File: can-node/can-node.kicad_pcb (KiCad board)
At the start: 4 copper layers, 76.3 x 58.9 mm, 139 parts, among them J1 Conn_ARM_JTAG_SWD_10, J2 Conn_01x04_Pin, J3 USART1, J4 Harwin M80-5402642, J5 Harwin M80-5402642, Q1 DMP510DL-7, SW1 KMR2, U1 TCAN3404-Q1, U10 TLV9101IDBVR, U11 TLV9101IDBVR, U12 TLV9101IDBVR, U13 TLV9101IDBVR, U14 TLV9101IDBVR, U15 TLV9101IDBVR, U16 TLV9101IDBVR, U17 TLV9101IDBVR, U18 TLV9101IDBVR, U19 TLV9101IDBVR, U2 STM32F105RBTx, U3 AP7375-33FDC, U4 TLV9101IDBVR, U5 TLV9101IDBVR, U6 TLV9101IDBVR, U7 TLV9101IDBVR, U8 TLV9101IDBVR, U9 TLV9101IDBVR, Y1 ECS-250-10-47Q-CES-TR

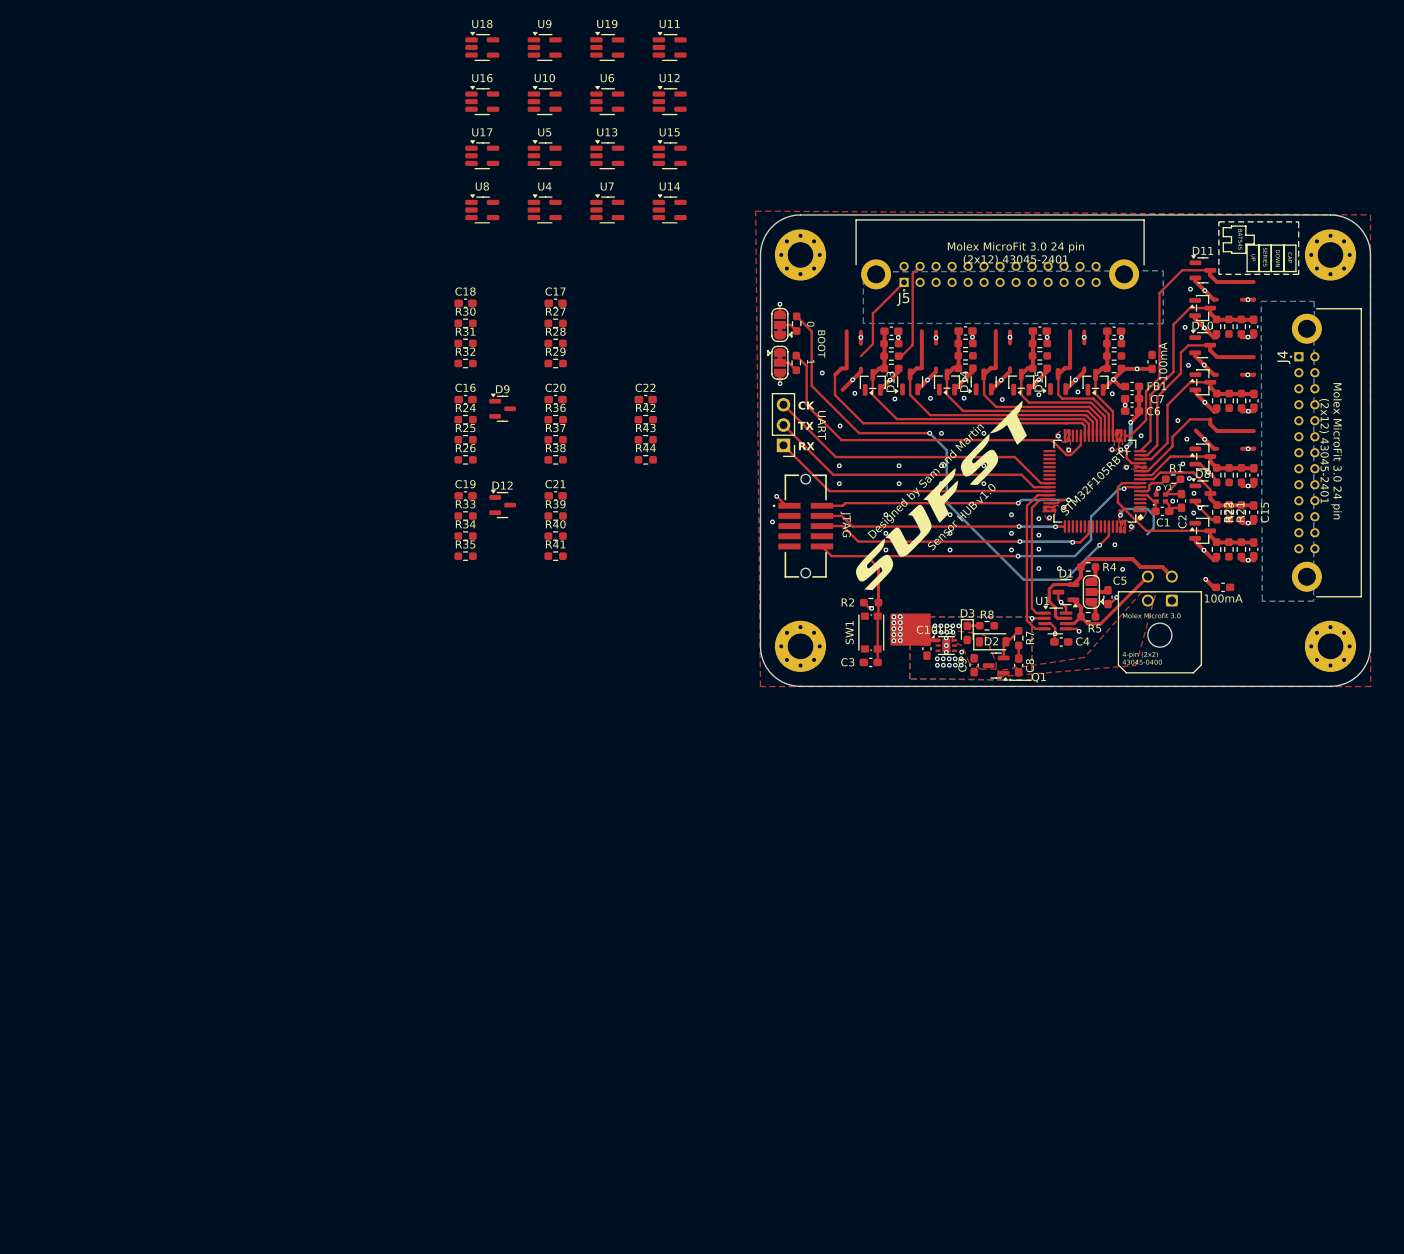
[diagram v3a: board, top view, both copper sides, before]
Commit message: reroute can-node
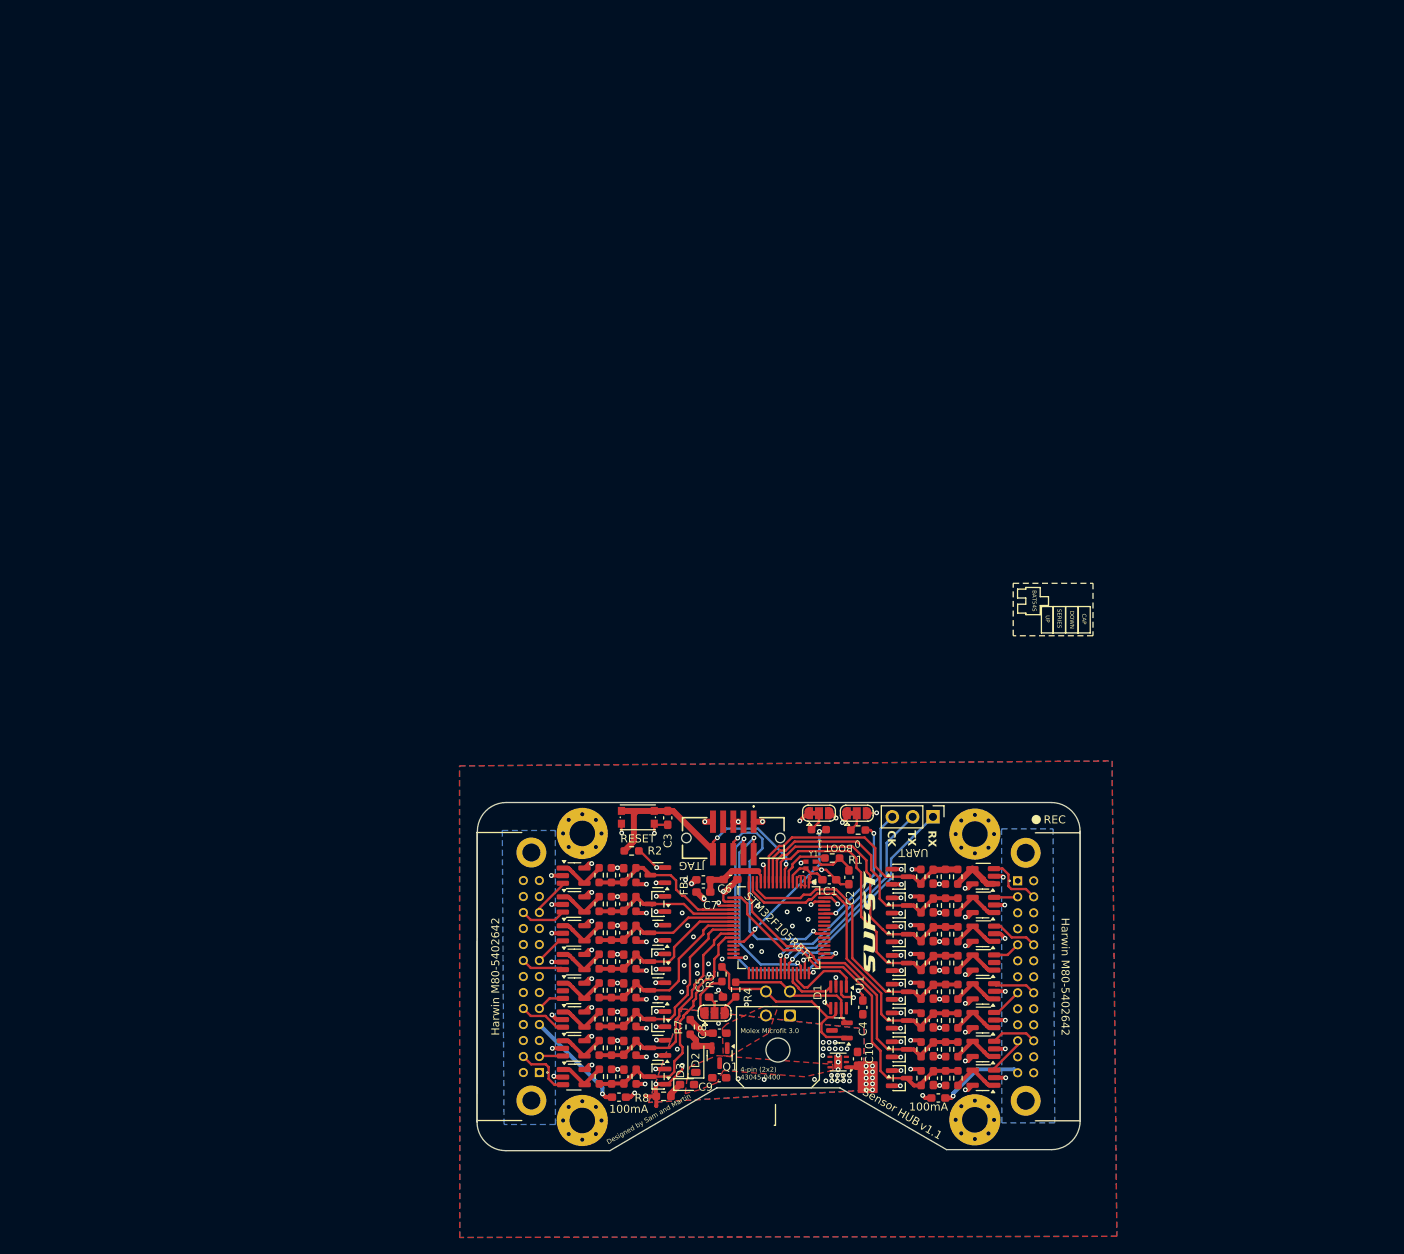
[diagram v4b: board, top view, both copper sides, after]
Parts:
- moved U11 134.6 mm to (144.4, 148.7), turned to 180 degrees
- moved U19 133.7 mm to (144.4, 145.1), turned to 180 degrees
- moved U18 127.3 mm to (144.4, 130.7), turned to 180 degrees
- moved U10 127.2 mm to (144.4, 141.5), turned to 180 degrees
- moved U9 126.8 mm to (144.4, 134.3), turned to 180 degrees
- moved U17 121.8 mm to (144.4, 137.9), turned to 180 degrees
- moved U12 118.9 mm to (93.2, 145.0)
- moved H2 118.2 mm to (94.3, 118.1), turned to 90 degrees
- moved U16 115.3 mm to (144.4, 123.5), turned to 180 degrees
- moved F2 113.5 mm to (98.9, 151.1), turned to 180 degrees
- moved H1 111.6 mm to (94.3, 154.0), turned to 90 degrees
- moved J5 108.8 mm to (88.9, 148.0), turned to -90 degrees
- moved U4 108.5 mm to (93.2, 148.6)
- moved U5 108.0 mm to (93.2, 141.4)
- moved U6 107.6 mm to (93.2, 134.2)
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- renumbered SW1 to RESET
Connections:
- U2 pad 10: /ADC_1_6 -> /ADC_1_0
- U2 pad 11: /ADC_1_2 -> /ADC_1_4
- U2 pad 14: /ADC_1_5 -> /ADC_1_6
- U2 pad 15: /ADC_1_1 -> /ADC_1_2
- U2 pad 16: /ADC_1_4 -> /ADC_1_7
- U2 pad 17: /ADC_1_0 -> /ADC_1_3
- U2 pad 20: /ADC_0_7 -> /ADC_0_3
- U2 pad 21: /ADC_0_3 -> /ADC_0_7
- U2 pad 22: /ADC_0_6 -> /ADC_0_2
- U2 pad 23: /ADC_0_2 -> /ADC_0_6
- U2 pad 24: /ADC_0_5 -> /ADC_0_1
- U2 pad 25: /ADC_0_1 -> /ADC_0_5
- U2 pad 26: /ADC_0_4 -> /ADC_0_0
- U2 pad 27: /ADC_0_0 -> /ADC_0_4
- U2 pad 8: /ADC_1_7 -> /ADC_1_1
- U2 pad 9: /ADC_1_3 -> /ADC_1_5
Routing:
- net GND: track 47.0 -> 104.9 mm, vias 98 -> 109
- net Net-(U2-BOOT0): track 63.9 -> 14.7 mm
- net /NReset: track 63.0 -> 35.6 mm
- net /ADC_1_3: track 16.8 -> 44.1 mm
- net Net-(U2-PB2): track 45.3 -> 19.9 mm, vias 0 -> 2
- net /ADC_1_2: track 18.5 -> 40.8 mm
- net /ADC_1_6: track 16.1 -> 37.1 mm
- net /ADC_1_7: track 24.3 -> 41.0 mm
- net /ADC_0_0: track 42.9 -> 28.3 mm
- net /CAN_RX: track 20.3 -> 6.65 mm
- net /ADC_1_5: track 21.9 -> 35.4 mm
- net /Generic ADC Input Group/3V3_FUSED: track 0.00 -> 13.3 mm, vias 0 -> 1
- net /ADC_0_1: track 34.8 -> 23.0 mm
- net /ADC_1_1: track 25.8 -> 37.3 mm
- net unconnected-(J5-Pin_1-Pad1): track 11.5 -> 0.00 mm
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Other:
- board size 76.3 x 58.9 mm -> 75.4 x 43.5 mm
- board text added: "Harwin M80-5402642"
- board text added: "REC"
- board text added: "v1.1"
- board text removed: "${REFERENCE}"
- board text removed: "Author: Antmicro"
- board text removed: "License: Apache-2.0"
- board text removed: "Molex MicroFit 3.0 24 pin (2x12) 43045-2401"
- board text removed: "v1.0"

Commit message: add silkscreen key to resistor generics
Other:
- board text added: "BUF"
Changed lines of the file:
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@@
 		(tags "capacitor handsolder")
 		(property "Reference" "C5"
-			(at -2.025 -1.5125 90)
+			(at 1.46 -0.86 180)
 			(layer "F.SilkS")
 			(effects
@@
 		(net 36)
 	)
+	(gr_rect
+		(start 105.642499 126.04)
+		(end 109.1375 140.92)
+		(stroke
+			(width 0.1)
+			(type default)
+		)
+		(fill no)
+		(layer "F.SilkS")
+	)
+	(gr_rect
+		(start 108.080728 139.590723)
+		(end 108.626417 140.585391)
+		(stroke
+			(width 0.1)
+			(type default)
+		)
+		(fill no)
+		(layer "F.SilkS")
+	)
+	(gr_rect
+		(start 107.14317 137.310192)
+		(end 107.685016 138.290723)
+		(stroke
+			(width 0.1)
+			(type default)
+		)
+		(fill no)
+		(layer "F.SilkS")
+	)
 	(gr_line
 		(start 118.42625 154.615)
@@
 		(layer "F.SilkS")
 	)
+	(gr_rect
+		(start 106.162915 139.590723)
+		(end 106.731661 140.585391)
+		(stroke
+			(width 0.1)
+			(type default)
+		)
+		(fill no)
+		(layer "F.SilkS")
+	)
+	(gr_rect
+		(start 105.965 134.159723)
+		(end 108.815 135.18)
+		(stroke
+			(width 0.1)
+			(type default)
+		)
+		(fill no)
+		(layer "F.SilkS")
+	)
 	(gr_line
 		(start 118.42625 154.615)
@@
 	)
 	(gr_rect
+		(start 106.015 132.65)
+		(end 108.765 133.656723)
+		(stroke
+			(width 0.1)
+			(type default)
+		)
+		(fill no)
+		(layer "F.SilkS")
+	)
+	(gr_rect
 		(start 153.132909 89.772692)
 		(end 154.685897 93.071054)
@@
 	)
 	(gr_rect
+		(start 106.14 126.3)
+		(end 108.64 130.51)
+		(stroke
+			(width 0.1)
+			(type default)
+		)
+		(fill no)
+		(layer "F.SilkS")
+	)
+	(gr_rect
+		(start 105.858517 138.290723)
+		(end 108.978517 139.590723)
+		(stroke
+			(width 0.1)
+			(type default)
+		)
+		(fill no)
+		(layer "F.SilkS")
+	)
+	(gr_rect
 		(start 148.13759 86.865738)
 		(end 158.115715 93.421668)
@@
 		(layer "F.SilkS")
 	)
+	(gr_rect
+		(start 106.01 131.076223)
+		(end 108.77 132.11)
+		(stroke
+			(width 0.1)
+			(type default)
+		)
+		(fill no)
+		(layer "F.SilkS")
+	)
 	(gr_poly
 		(pts
@@
 		(layer "F.SilkS")
 	)
+	(gr_rect
+		(start 105.995 135.75)
+		(end 108.785 136.67)
+		(stroke
+			(width 0.1)
+			(type default)
+		)
+		(fill no)
+		(layer "F.SilkS")
+	)
 	(gr_line
 		(start 111.09 149.94)
@@
 		)
 	)
-	(gr_text "UP"
-		(at 152.139852 90.852206 270)
+	(gr_text "Harwin M80-5402642"
+		(at 84.015 136.02 90)
 		(layer "F.SilkS")
 		(effects
 			(font
-				(size 0.5 0.5)
+				(size 1 1)
 				(thickness 0.1)
 			)
-			(justify left bottom)
+			(justify bottom)
 		)
 	)
-	(gr_text "Harwin M80-5402642"
-		(at 84.015 136.02 90)
+	(gr_text "CAP"
+		(at 106.575714 135.008965 0)
 		(layer "F.SilkS")
 		(effects
 			(font
-				(size 1 1)
+				(size 0.5 0.5)
 				(thickness 0.1)
 			)
-			(justify bottom)
+			(justify left bottom)
 		)
 	)
@@
 		)
 	)
-	(gr_text "BAT54S"
-		(at 150.489852 87.724825 270)
-		(layer "F.SilkS")
-		(effects
-			(font
-				(size 0.5 0.5)
-				(thickness 0.1)
-			)
-			(justify left bottom)
-		)
-	)
 	(gr_text "UART"
 		(at 137.543333 119.969859 180)
@@
 		)
 	)
+	(gr_text "BUF"
+		(at 106.8505 126.897321 270)
+		(layer "F.SilkS")
+		(effects
+			(font
+				(size 1 1)
+				(thickness 0.1)
+			)
+			(justify left bottom)
+		)
+	)
 	(gr_text "CK"
 		(at 132.33625 117.744859 270)
@@
 		)
 	)
-	(gr_text "SERIES"
-		(at 153.614852 90.066492 270)
+	(gr_text "UP"
+		(at 106.778095 136.526423 0)
 		(layer "F.SilkS")
 		(effects
@@
 		)
 	)
-	(gr_text "0"
-		(at 129.075 118.91 180)
+	(gr_text "BAT54S"
+		(at 105.920953 139.26952 0)
 		(layer "F.SilkS")
 		(effects
 			(font
-				(size 0.9 0.9)
+				(size 0.5 0.5)
 				(thickness 0.1)
 			)
@@
 		)
 	)
-	(gr_text "CAP"
-		(at 156.714852 90.649825 270)
+	(gr_text "0"
+		(at 129.075 118.91 180)
 		(layer "F.SilkS")
 		(effects
 			(font
-				(size 0.5 0.5)
+				(size 0.9 0.9)
 				(thickness 0.1)
 			)
@@
 		)
 	)
-	(gr_text "DOWN"
-		(at 155.189852 90.304586 270)
+	(gr_text "SERIES"
+		(at 105.992381 131.915685 0)
 		(layer "F.SilkS")
 		(effects
@@
 		)
 	)
+	(gr_text "DOWN"
+		(at 106.230475 133.472052 0)
+		(layer "F.SilkS")
+		(effects
+			(font
+				(size 0.5 0.5)
+				(thickness 0.1)
+			)
+			(justify left bottom)
+		)
+	)
 	(segment
 		(start 128.586429 116.96)
@@
 	)
 	(group ""
-		(members "0edcd34a-debb-45da-8952-579d34b4af57" "4663f03b-6618-4a83-a739-2cb0ab0a32b1"
-			"90cc401b-1bde-4182-a633-3583f1a28334" "93d07e56-6b9b-4ff7-b93a-5dea41abb8df"
-			"a9ef13ed-728d-4903-8032-7c7617360637" "aaba5aea-e0d1-48a4-904b-a5e3b1491da8"
-			"bb697296-451f-4846-8e61-99af6237f61b" "ce363793-6118-46f4-806a-0781e1e8ee00"
-			"d2c4a6f1-e2ac-4784-970b-23c93171d1e9" "ebb9684b-553b-4642-b1c8-c1a5ef15ab38"
-			"f4929926-5439-4c27-8a2d-6f5ef2494bde"
+		(members "90cc401b-1bde-4182-a633-3583f1a28334" "a9ef13ed-728d-4903-8032-7c7617360637"
+			"aaba5aea-e0d1-48a4-904b-a5e3b1491da8" "d2c4a6f1-e2ac-4784-970b-23c93171d1e9"
+			"ebb9684b-553b-4642-b1c8-c1a5ef15ab38" "f4929926-5439-4c27-8a2d-6f5ef2494bde"
 		)
 	)

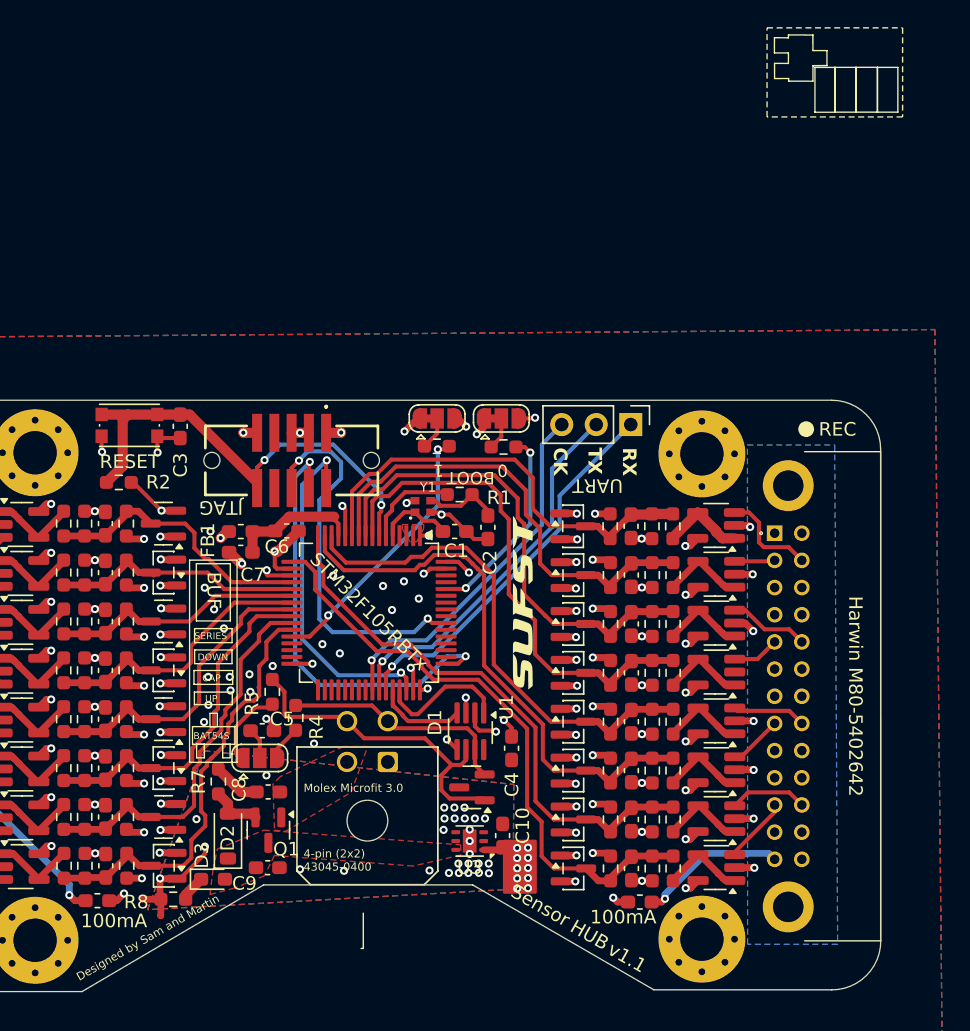
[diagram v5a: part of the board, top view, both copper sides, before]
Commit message: fix some silkscreen issues + add more vias
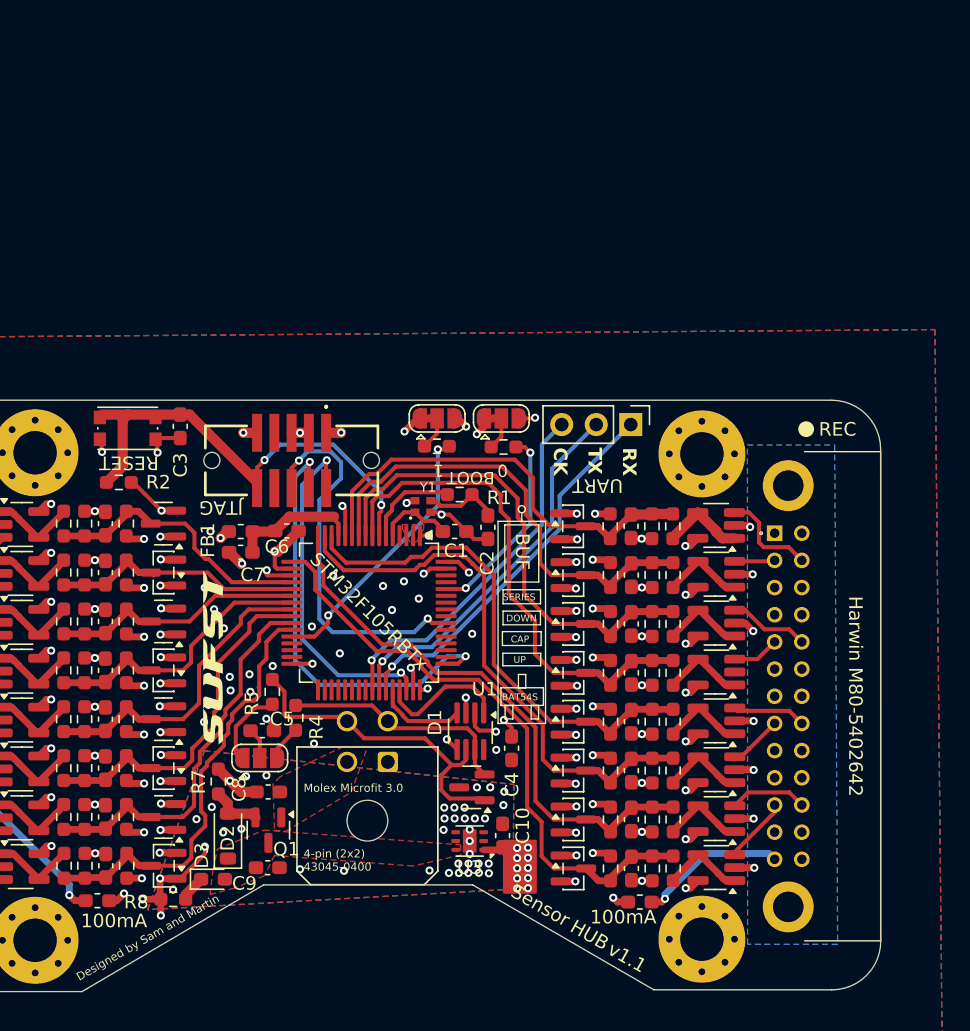
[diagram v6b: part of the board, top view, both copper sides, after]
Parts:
- removed RESET: KMR2, Button_Switch_SMD:SW_Push_1P1T_NO_CK_KMR2
- added SW1: RESET, Button_Switch_SMD:SW_Push_1P1T_NO_CK_KMR2, F.Cu at (101.1, 116.3)
- moved G*** 23.2 mm to (107.3, 133.2)
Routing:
- net GND: track 104.9 -> 103.8 mm, vias 109 -> 123
- net /CANL: track 24.4 -> 23.8 mm
- net +3V3: track 76.6 -> 76.1 mm
